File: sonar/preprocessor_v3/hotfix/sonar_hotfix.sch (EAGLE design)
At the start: 1 part

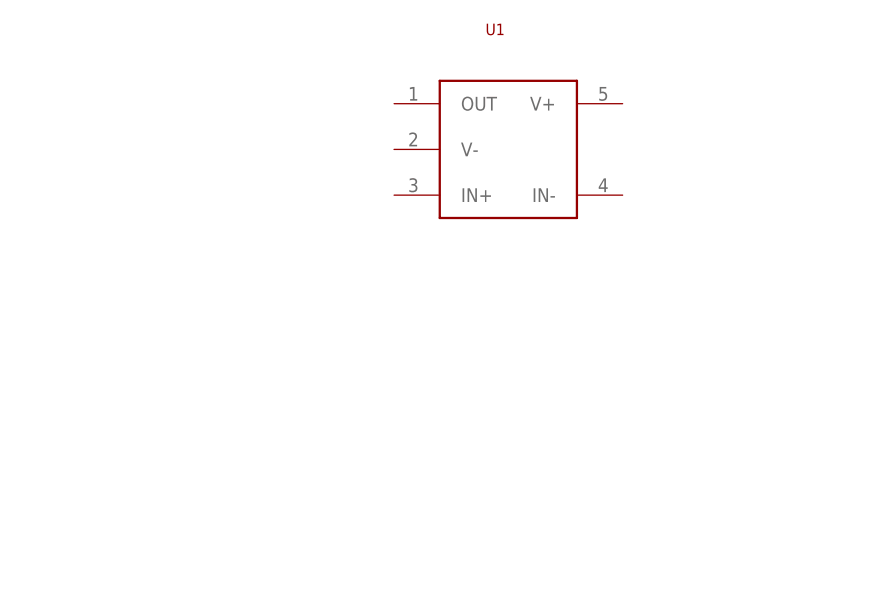
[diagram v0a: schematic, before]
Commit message: Designed and laid out buffer circuit
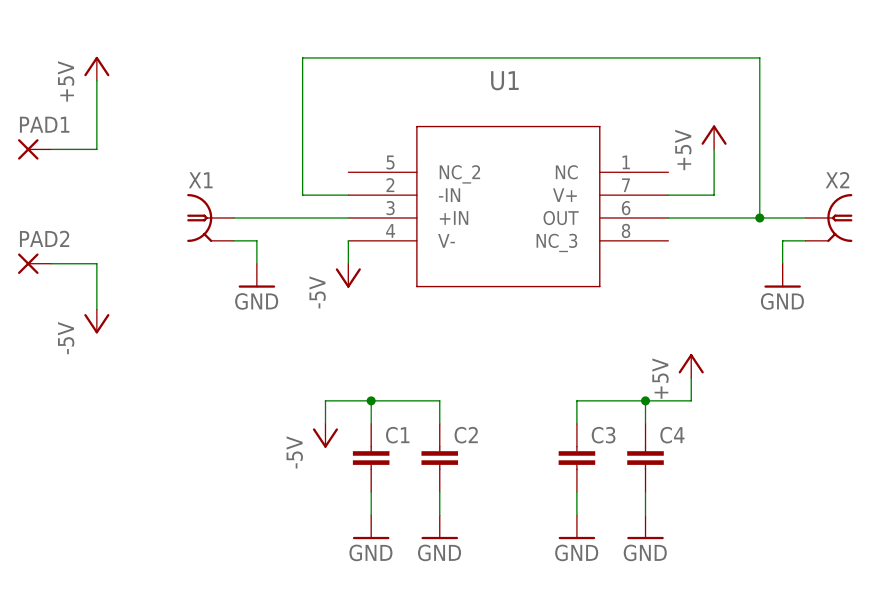
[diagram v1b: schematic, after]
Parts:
- added C1, C2, C3, C4: (no value), rcl:C-EUC0603
- added PAD1, PAD2: WIREPADSMD5-2,5, wirepad:WIREPADSMD5-2,5
- added X1, X2: (no value), hotfix:0731000105
- U1: device hotfix:LTC6240 -> hotfix:LTC6240SO-8
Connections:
- new net +5V: C3.1, C4.1, PAD1.P, U1.V+
- new net -5V: C1.1, C2.1, PAD2.P, U1.V-
- new net GND: C1.2, C2.2, C3.2, C4.2, X1.2, X2.2
- new net N$1: U1.+IN, X1.1
- new net N$2: U1.-IN, U1.OUT, X2.1
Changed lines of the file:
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@@
 </classes>
 <parts>
-<part name="U1" library="hotfix" deviceset="LTC6240" device=""/>
+<part name="U1" library="hotfix" deviceset="LTC6240" device="SO-8"/>
+<part name="X1" library="hotfix" deviceset="0731000105" device=""/>
+<part name="X2" library="hotfix" deviceset="0731000105" device=""/>
+<part name="P+1" library="supply1" library_urn="urn:adsk.eagle:library:371" deviceset="+5V" device=""/>
+<part name="P-1" library="supply1" library_urn="urn:adsk.eagle:library:371" deviceset="-5V" device=""/>
+<part name="PAD1" library="wirepad" library_urn="urn:adsk.eagle:library:412" deviceset="WIREPAD" device="SMD5-2,5" package3d_urn="urn:adsk.eagle:package:30845/1"/>
+<part name="PAD2" library="wirepad" library_urn="urn:adsk.eagle:library:412" deviceset="WIREPAD" device="SMD5-2,5" package3d_urn="urn:adsk.eagle:package:30845/1"/>
+<part name="P+2" library="supply1" library_urn="urn:adsk.eagle:library:371" deviceset="+5V" device=""/>
+<part name="P-2" library="supply1" library_urn="urn:adsk.eagle:library:371" deviceset="-5V" device=""/>
+<part name="C1" library="rcl" library_urn="urn:adsk.eagle:library:334" deviceset="C-EU" device="C0603" package3d_urn="urn:adsk.eagle:package:23616/2"/>
+<part name="C2" library="rcl" library_urn="urn:adsk.eagle:library:334" deviceset="C-EU" device="C0603" package3d_urn="urn:adsk.eagle:package:23616/2"/>
+<part name="C3" library="rcl" library_urn="urn:adsk.eagle:library:334" deviceset="C-EU" device="C0603" package3d_urn="urn:adsk.eagle:package:23616/2"/>
+<part name="C4" library="rcl" library_urn="urn:adsk.eagle:library:334" deviceset="C-EU" device="C0603" package3d_urn="urn:adsk.eagle:package:23616/2"/>
+<part name="GND1" library="supply1" library_urn="urn:adsk.eagle:library:371" deviceset="GND" device=""/>
+<part name="GND2" library="supply1" library_urn="urn:adsk.eagle:library:371" deviceset="GND" device=""/>
+<part name="GND3" library="supply1" library_urn="urn:adsk.eagle:library:371" deviceset="GND" device=""/>
+<part name="GND4" library="supply1" library_urn="urn:adsk.eagle:library:371" deviceset="GND" device=""/>
+<part name="GND5" library="supply1" library_urn="urn:adsk.eagle:library:371" deviceset="GND" device=""/>
+<part name="GND6" library="supply1" library_urn="urn:adsk.eagle:library:371" deviceset="GND" device=""/>
+<part name="P-3" library="supply1" library_urn="urn:adsk.eagle:library:371" deviceset="-5V" device=""/>
+<part name="P+3" library="supply1" library_urn="urn:adsk.eagle:library:371" deviceset="+5V" device=""/>
 </parts>
 <sheets>
@@
 <instances>
 <instance part="U1" gate="G$1" x="0" y="0"/>
+<instance part="X1" gate="G$1" x="-33.02" y="0"/>
+<instance part="X2" gate="G$1" x="35.56" y="0" rot="MR0"/>
+<instance part="P+1" gate="1" x="22.86" y="10.16"/>
+<instance part="P-1" gate="1" x="-17.78" y="-7.62"/>
+<instance part="PAD1" gate="G$1" x="-53.34" y="7.62" smashed="yes">
+<attribute name="NAME" x="-54.483" y="9.4742" size="1.778" layer="95"/>
+</instance>
+<instance part="PAD2" gate="G$1" x="-53.34" y="-5.08" smashed="yes">
+<attribute name="NAME" x="-54.483" y="-3.2258" size="1.778" layer="95"/>
+</instance>
+<instance part="P+2" gate="1" x="-45.72" y="17.78"/>
+<instance part="P-2" gate="1" x="-45.72" y="-12.7"/>
+<instance part="C1" gate="G$1" x="-15.24" y="-25.4"/>
+<instance part="C2" gate="G$1" x="-7.62" y="-25.4"/>
+<instance part="C3" gate="G$1" x="7.62" y="-25.4"/>
+<instance part="C4" gate="G$1" x="15.24" y="-25.4"/>
+<instance part="GND1" gate="1" x="30.48" y="-7.62"/>
+<instance part="GND2" gate="1" x="-27.94" y="-7.62"/>
+<instance part="GND3" gate="1" x="7.62" y="-35.56"/>
+<instance part="GND4" gate="1" x="15.24" y="-35.56"/>
+<instance part="GND5" gate="1" x="-7.62" y="-35.56"/>
+<instance part="GND6" gate="1" x="-15.24" y="-35.56"/>
+<instance part="P-3" gate="1" x="-20.32" y="-25.4"/>
+<instance part="P+3" gate="1" x="20.32" y="-15.24"/>
 </instances>
 <busses>
 </busses>
 <nets>
+<net name="N$1" class="0">
+<segment>
+<pinref part="X1" gate="G$1" pin="1"/>
+<pinref part="U1" gate="G$1" pin="+IN"/>
+<wire x1="-30.48" y1="0" x2="-17.78" y2="0" width="0.1524" layer="91"/>
+</segment>
+</net>
+<net name="N$2" class="0">
+<segment>
+<pinref part="U1" gate="G$1" pin="OUT"/>
+<pinref part="X2" gate="G$1" pin="1"/>
+<wire x1="17.78" y1="0" x2="27.94" y2="0" width="0.1524" layer="91"/>
+<wire x1="27.94" y1="0" x2="33.02" y2="0" width="0.1524" layer="91"/>
+<wire x1="27.94" y1="0" x2="27.94" y2="17.78" width="0.1524" layer="91"/>
+<wire x1="27.94" y1="17.78" x2="-22.86" y2="17.78" width="0.1524" layer="91"/>
+<wire x1="-22.86" y1="17.78" x2="-22.86" y2="2.54" width="0.1524" layer="91"/>
+<pinref part="U1" gate="G$1" pin="-IN"/>
+<wire x1="-22.86" y1="2.54" x2="-17.78" y2="2.54" width="0.1524" layer="91"/>
+<junction x="27.94" y="0"/>
+</segment>
+</net>
+<net name="+5V" class="0">
+<segment>
+<pinref part="U1" gate="G$1" pin="V+"/>
+<wire x1="17.78" y1="2.54" x2="22.86" y2="2.54" width="0.1524" layer="91"/>
+<wire x1="22.86" y1="2.54" x2="22.86" y2="7.62" width="0.1524" layer="91"/>
+<pinref part="P+1" gate="1" pin="+5V"/>
+</segment>
+<segment>
+<pinref part="P+2" gate="1" pin="+5V"/>
+<wire x1="-45.72" y1="15.24" x2="-45.72" y2="7.62" width="0.1524" layer="91"/>
+<pinref part="PAD1" gate="G$1" pin="P"/>
+<wire x1="-45.72" y1="7.62" x2="-50.8" y2="7.62" width="0.1524" layer="91"/>
+</segment>
+<segment>
+<pinref part="P+3" gate="1" pin="+5V"/>
+<wire x1="20.32" y1="-17.78" x2="20.32" y2="-20.32" width="0.1524" layer="91"/>
+<pinref part="C3" gate="G$1" pin="1"/>
+<wire x1="7.62" y1="-22.86" x2="7.62" y2="-20.32" width="0.1524" layer="91"/>
+<wire x1="7.62" y1="-20.32" x2="15.24" y2="-20.32" width="0.1524" layer="91"/>
+<pinref part="C4" gate="G$1" pin="1"/>
+<wire x1="15.24" y1="-20.32" x2="15.24" y2="-22.86" width="0.1524" layer="91"/>
+<wire x1="20.32" y1="-20.32" x2="15.24" y2="-20.32" width="0.1524" layer="91"/>
+<junction x="15.24" y="-20.32"/>
+</segment>
+</net>
+<net name="-5V" class="0">
+<segment>
+<pinref part="U1" gate="G$1" pin="V-"/>
+<wire x1="-17.78" y1="-2.54" x2="-17.78" y2="-5.08" width="0.1524" layer="91"/>
+<pinref part="P-1" gate="1" pin="-5V"/>
+</segment>
+<segment>
+<pinref part="PAD2" gate="G$1" pin="P"/>
+<wire x1="-50.8" y1="-5.08" x2="-45.72" y2="-5.08" width="0.1524" layer="91"/>
+<pinref part="P-2" gate="1" pin="-5V"/>
+<wire x1="-45.72" y1="-5.08" x2="-45.72" y2="-10.16" width="0.1524" layer="91"/>
+</segment>
+<segment>
+<pinref part="P-3" gate="1" pin="-5V"/>
+<wire x1="-20.32" y1="-22.86" x2="-20.32" y2="-20.32" width="0.1524" layer="91"/>
+<pinref part="C2" gate="G$1" pin="1"/>
+<wire x1="-7.62" y1="-22.86" x2="-7.62" y2="-20.32" width="0.1524" layer="91"/>
+<wire x1="-7.62" y1="-20.32" x2="-15.24" y2="-20.32" width="0.1524" layer="91"/>
+<pinref part="C1" gate="G$1" pin="1"/>
+<wire x1="-15.24" y1="-20.32" x2="-15.24" y2="-22.86" width="0.1524" layer="91"/>
+<wire x1="-20.32" y1="-20.32" x2="-15.24" y2="-20.32" width="0.1524" layer="91"/>
+<junction x="-15.24" y="-20.32"/>
+</segment>
+</net>
+<net name="GND" class="0">
+<segment>
+<pinref part="X2" gate="G$1" pin="2"/>
+<wire x1="33.02" y1="-2.54" x2="30.48" y2="-2.54" width="0.1524" layer="91"/>
+<wire x1="30.48" y1="-2.54" x2="30.48" y2="-5.08" width="0.1524" layer="91"/>
+<pinref part="GND1" gate="1" pin="GND"/>
+</segment>
+<segment>
+<pinref part="X1" gate="G$1" pin="2"/>
+<wire x1="-30.48" y1="-2.54" x2="-27.94" y2="-2.54" width="0.1524" layer="91"/>
+<wire x1="-27.94" y1="-2.54" x2="-27.94" y2="-5.08" width="0.1524" layer="91"/>
+<pinref part="GND2" gate="1" pin="GND"/>
+</segment>
+<segment>
+<pinref part="C1" gate="G$1" pin="2"/>
+<pinref part="GND6" gate="1" pin="GND"/>
+<wire x1="-15.24" y1="-30.48" x2="-15.24" y2="-33.02" width="0.1524" layer="91"/>
+</segment>
+<segment>
+<pinref part="C2" gate="G$1" pin="2"/>
+<pinref part="GND5" gate="1" pin="GND"/>
+<wire x1="-7.62" y1="-30.48" x2="-7.62" y2="-33.02" width="0.1524" layer="91"/>
+</segment>
+<segment>
+<pinref part="C3" gate="G$1" pin="2"/>
+<pinref part="GND3" gate="1" pin="GND"/>
+<wire x1="7.62" y1="-30.48" x2="7.62" y2="-33.02" width="0.1524" layer="91"/>
+</segment>
+<segment>
+<pinref part="C4" gate="G$1" pin="2"/>
+<pinref part="GND4" gate="1" pin="GND"/>
+<wire x1="15.24" y1="-30.48" x2="15.24" y2="-33.02" width="0.1524" layer="91"/>
+</segment>
+</net>
 </nets>
 </sheet>
@@
 </drawing>
 <compatibility>
+<note version="8.2" severity="warning">
+Since Version 8.2, EAGLE supports online libraries. The ids
+of those online libraries will not be understood (or retained)
+with this version.
+</note>
 <note version="8.3" severity="warning">
 Since Version 8.3, EAGLE supports URNs for individual library
@@
 will not be understood (or retained) with this version.
 </note>
+<note version="8.3" severity="warning">
+Since Version 8.3, EAGLE supports the association of 3D packages
+with devices in libraries, schematics, and board files. Those 3D
+packages will not be understood (or retained) with this version.
+</note>
+<note version="8.4" severity="warning">
+Since Version 8.4, EAGLE supports properties for SPICE simulation.
+Probes in schematics and SPICE mapping objects found in parts and library devices
+will not be understood with this version. Update EAGLE to the latest version
+for full support of SPICE simulation.
+</note>
 </compatibility>
